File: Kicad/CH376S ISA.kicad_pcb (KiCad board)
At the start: 2 copper layers, 104 x 73.9 mm, 28 parts, among them J1 Bus_ISA_8bit, J2 ROM CS, U1 CH376, U13 74LS138, U14 74LS138, U15 74LS138, U2 LM1117-3.3, U3 28C256, U4 74LS138, U5 74LS138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

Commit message: update
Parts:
- added J3: ROM CS, Connector_PinHeader_2.54mm:PinHeader_2x02_P2.54mm_Vertical, F.Cu at (162.8, 89.4)
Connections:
- U4 pad 1: /A17 -> /A16
- U4 pad 10: Net-(U4-Pad10) -> /ROM_CS_0XDX
- U4 pad 2: /A18 -> /A17
- U4 pad 3: /A19 -> /A18
- U4 pad 4: /A16 -> /GND
- U4 pad 7: /ROM_CS_0XEX -> Net-(U4-Pad7)
- U4 pad 9: Net-(U4-Pad9) -> /ROM_CS_0XEX
- U5 pad 4: /ROM_CS_0XEX -> /ROM_CS_E_D
- U5 pad 6: /5+ -> /A19
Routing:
- net /ROM_CS_0XDX: track 0.00 -> 63.1 mm, vias 0 -> 2
- net /A19: track 31.7 -> 94.2 mm, vias 2 -> 3
- net /ROM_CS_E_D: track 0.00 -> 27.3 mm, vias 0 -> 2
- net /5+: track 313.2 -> 289.1 mm, vias 12 -> 10
- net /ROM_CS_0XEX: track 88.6 -> 65.2 mm, vias 3 -> 2
- net /GND: track 399.3 -> 412.3 mm, vias 17 -> 19
- net /A16: track 26.2 -> 33.8 mm
- net /A17: track 33.8 -> 31.5 mm
- net /A18: track 32.7 -> 30.4 mm
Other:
- board text added: "0XD_..."
- board text added: "0XE_..."
- board text added: "0X_0..."
- board text added: "0X_2..."
- board text added: "0X_4..."
- board text added: "0X_6..."
- board text added: "0X_8..."
- board text added: "0X_A..."
- board text added: "0X_C..."
- board text added: "0X_E..."
- board text removed: "0XE0..."
- board text removed: "0XE2..."
- board text removed: "0XE4..."
- board text removed: "0XE6..."
- board text removed: "0XE8..."
- board text removed: "0XEA..."
- board text removed: "0XEC..."
- board text removed: "0XEE..."

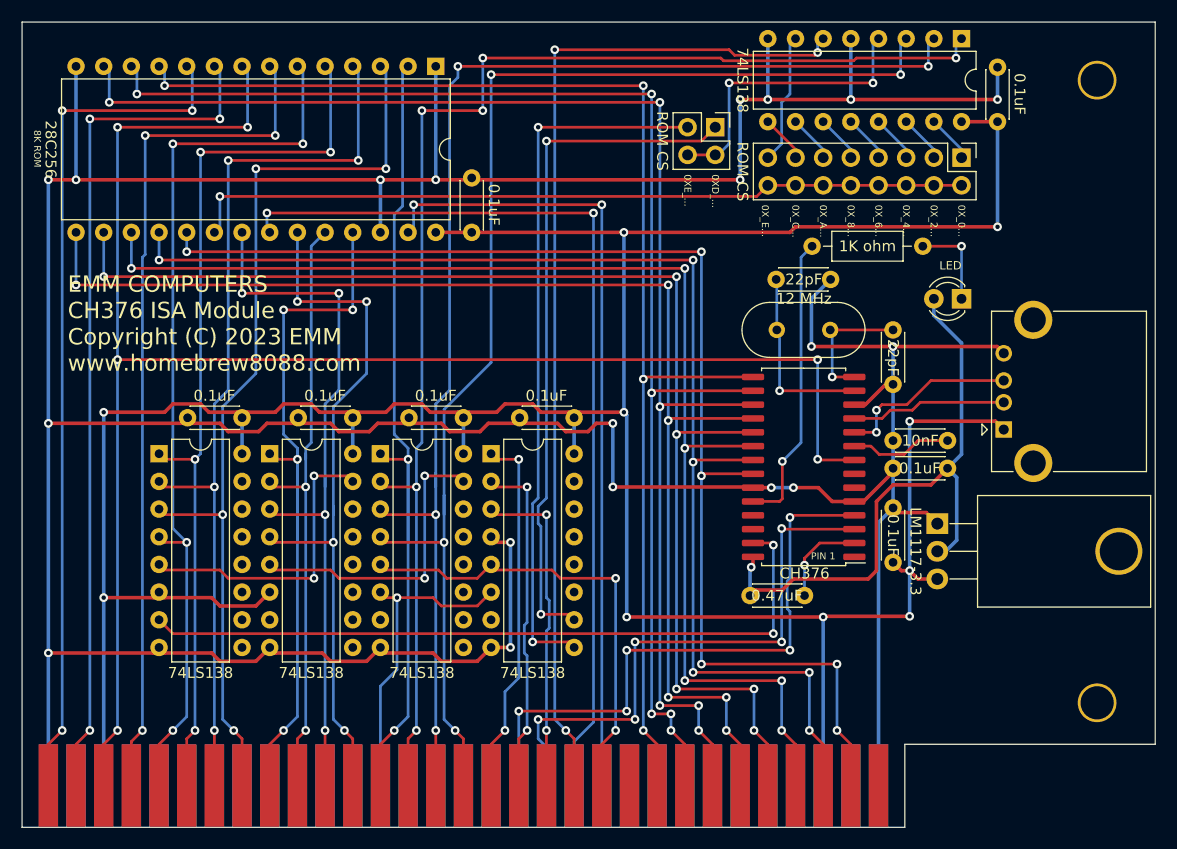
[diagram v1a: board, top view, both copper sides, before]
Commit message: Changed IO address to 0x07E0
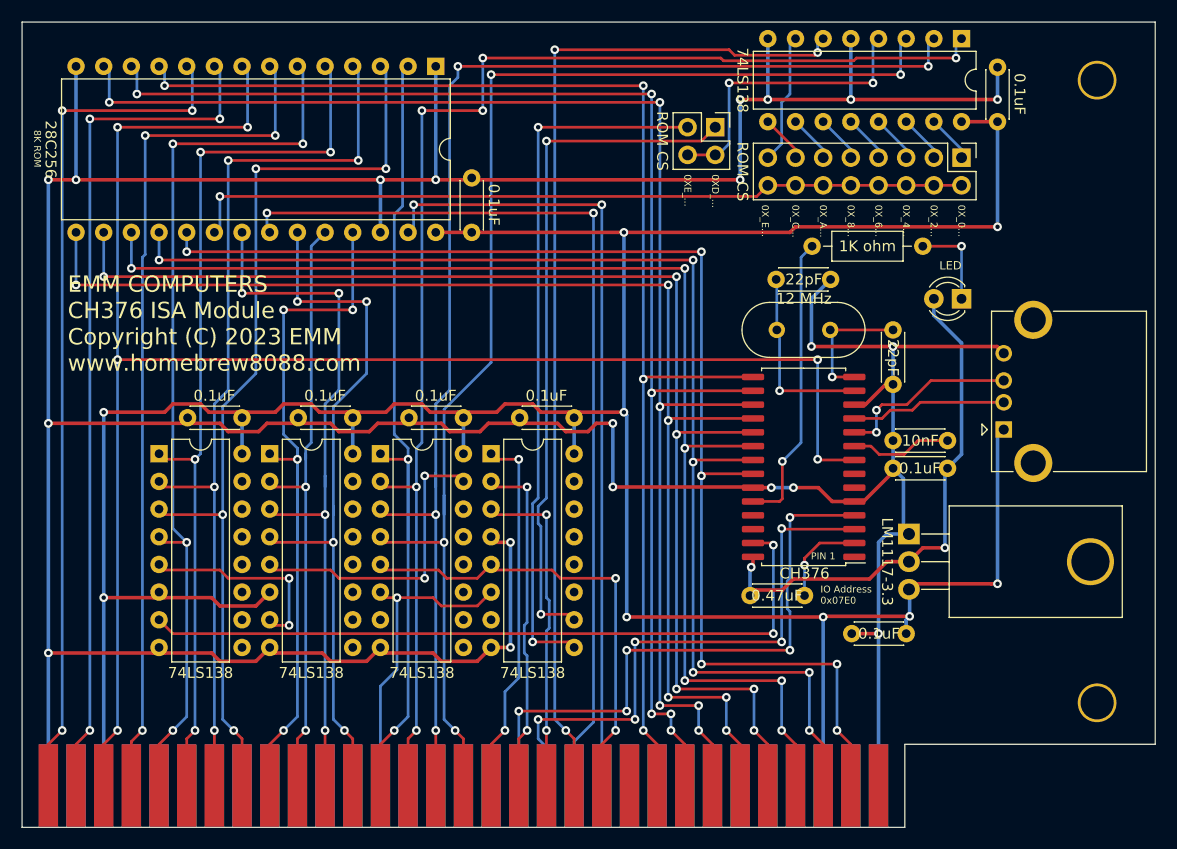
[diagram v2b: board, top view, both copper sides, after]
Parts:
- moved C6 6.65 mm to (180.3, 135.9), turned to 180 degrees
- moved U2 2.77 mm to (180.6, 126.7)
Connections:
- U14 pad 7: Net-(U14-Pad7) -> /IO_07XX
- U15 pad 5: /IO_00XX -> /IO_07XX
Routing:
- net /IO_00XX: track 27.9 -> 0.00 mm, vias 2 -> 0
- net /IO_07XX: track 0.00 -> 18.8 mm, vias 0 -> 2
- net /3v3: track 56.7 -> 48.0 mm, vias 1 -> 2
- net /5+: track 289.1 -> 284.5 mm, vias 10 -> 9
- net /GND: track 412.3 -> 412.4 mm, vias 19 -> 20
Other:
- board text added: "IO Address 0x07E0"
